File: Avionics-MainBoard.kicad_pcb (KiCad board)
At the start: 4 copper layers, 90.2 x 95.9 mm, 268 parts, among them J1 USB_C_Receptacle_USB2.0, J10 1824543, J11 1824527, J12 1824527, J13 1824527, J14 200528-0100, J15 200528-0100, J16 200528-0100, J17 1824543, J18 200528-0100, J19 200528-0100, J2 200528-0100, J3 Conn_01x06, J4 200528-0100, J5 Micro_SD_Card_Det2, J6 200528-0100, J7 U.FL-R-SMT-1, J8 Conn_01x02, J9 200528-0100, Q1 IRLML2803, Q10 MBT2222ADW1T1, Q11 MBT2222ADW1T1, Q12 MBT2222ADW1T1, Q13 MBT2222ADW1T1, Q14 MMBT2907, Q15 MMBT2907, Q16 NX3008NBKS, Q17 MBT2222ADW1T1, Q2 MBT2222ADW1T1, Q22 NX3008NBKS, Q24 NX3008NBKS, Q26 NX3008NBKS, Q28 NX3008NBKS, Q29 MBT2222ADW1T1, Q3 MBT2222ADW1T1, Q30 MBT2222ADW1T1, Q4 NX3008NBKS, Q44 NX3008NBKS, Q46 NX3008NBKS, Q48 NX3008NBKS, Q5 MBT2222ADW1T1, Q50 NX3008NBKS, Q52 NX3008NBKS, Q6 MBT2222ADW1T1, Q7 MBT2222ADW1T1, Q8 MBT2222ADW1T1, Q9 MBT2222ADW1T1, Q99 NX3008NBKS, SW1 SW_Omron_B3FS, SW2 SW_Omron_B3FS, U1 MR25H40MDF, U10 BTS5090-1EJA, U12 ADM1491EBR, U14 ADM1176-1ARMZ-R7, U15 TPS7A4501DCQT, U16 ADM1176-1ARMZ-R7, U17 TPS54226PWPR, U18 ADM1176-1ARMZ-R7, U2 RP2040, U3 MAX706RESA+, U4 DS3231M, U5 BNO085, U6 USBLC6-2SC6, U7 E22-900M30S, U8 S1216V8, U9 BQ25883RGER, Y1 12MHz, Y2 32.768kHz

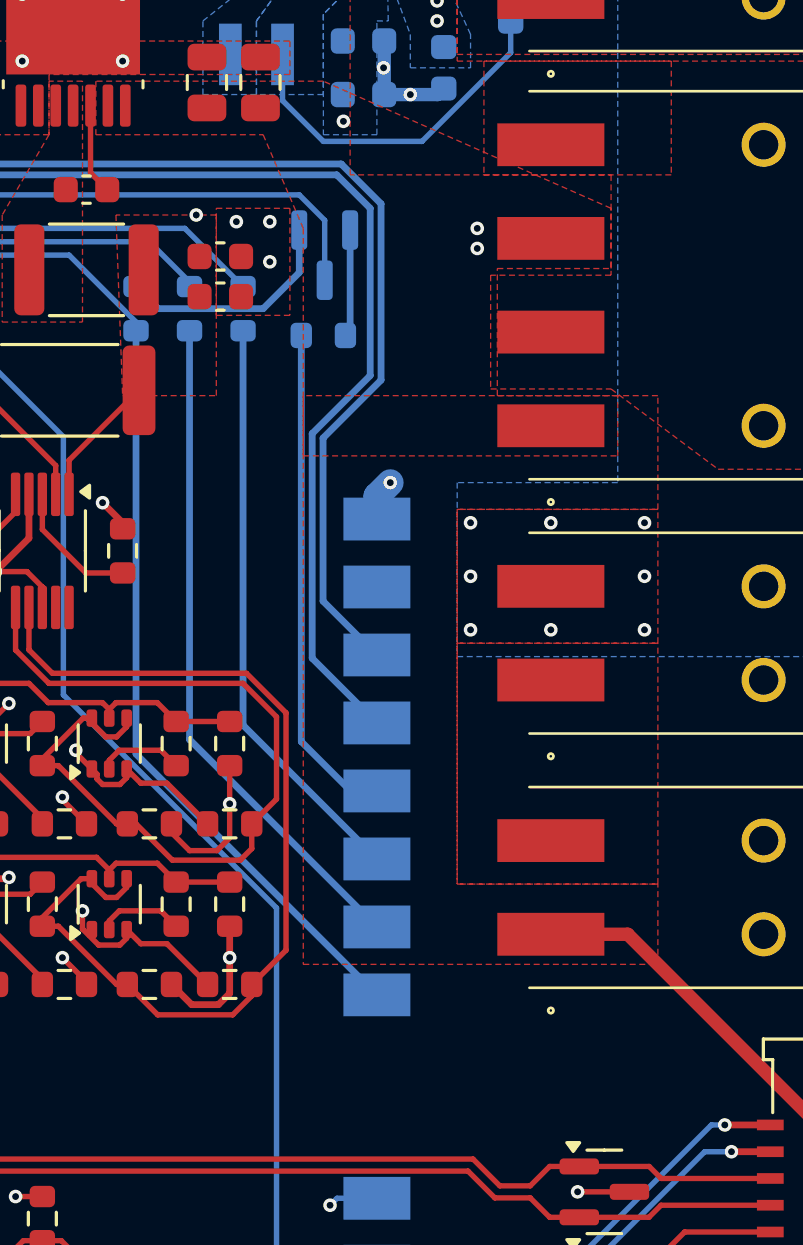
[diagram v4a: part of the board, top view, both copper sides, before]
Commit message: Silkscreen hiding
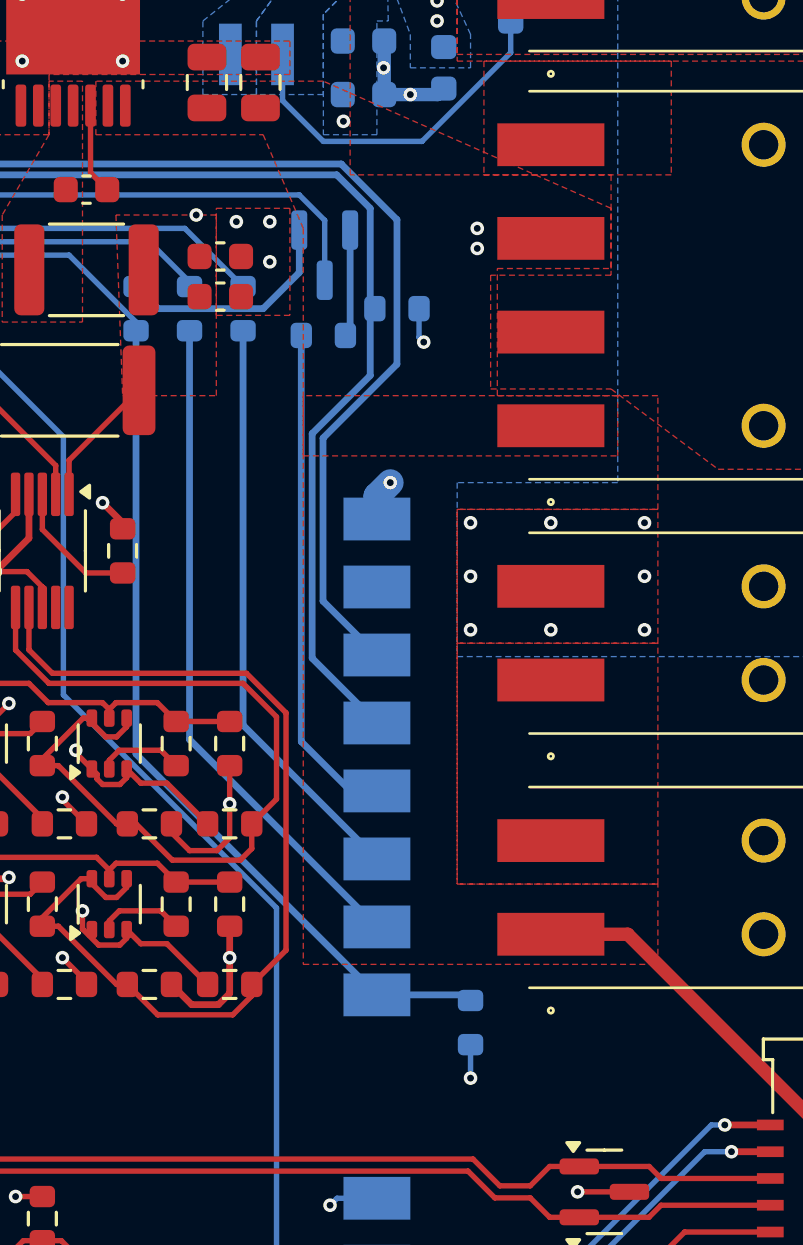
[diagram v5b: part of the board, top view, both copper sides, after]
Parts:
- added R34: 10K, Resistor_SMD:R_0603_1608Metric, B.Cu at (175.2, 95.0)
- added R35: 10K, Resistor_SMD:R_0603_1608Metric, B.Cu at (178.0, 121.7)
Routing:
- net /LoRa Power/LoRa_CSn: track 48.6 -> 52.2 mm
- net +3V3: track 180.1 -> 182.6 mm, vias 65 -> 67

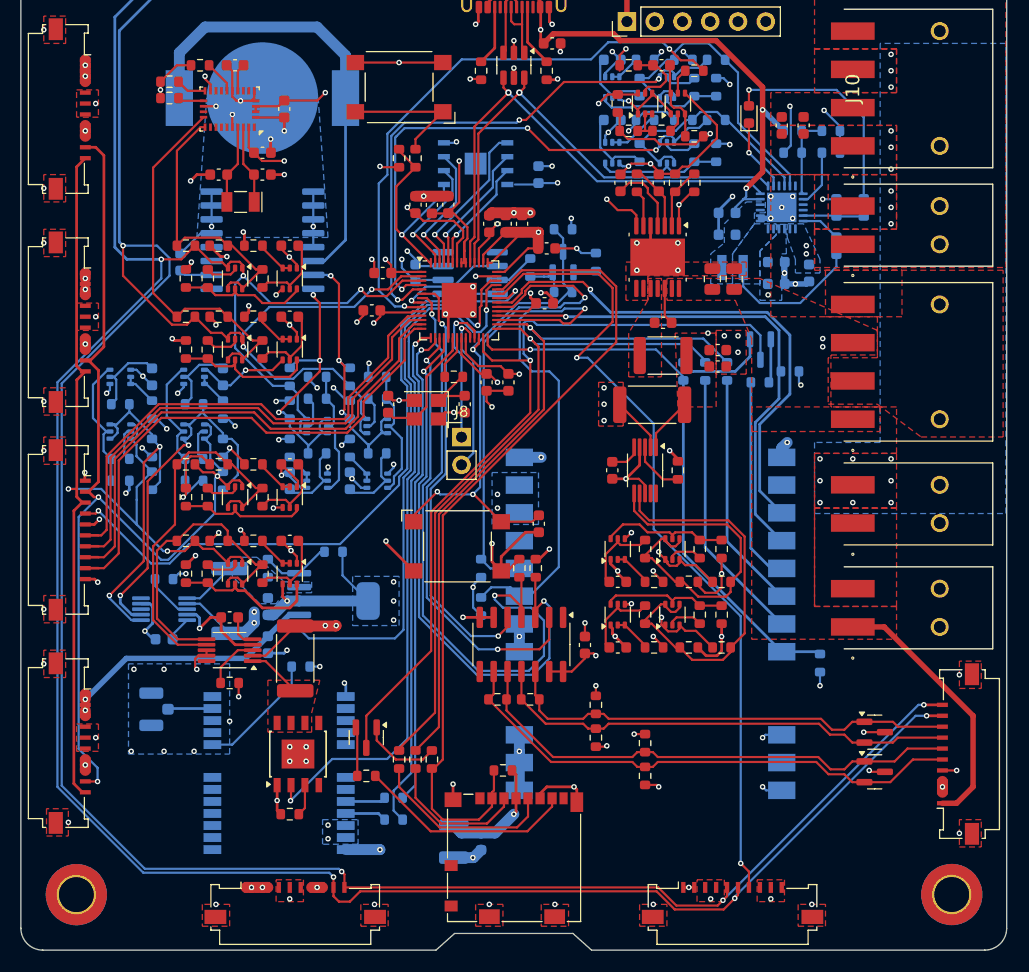
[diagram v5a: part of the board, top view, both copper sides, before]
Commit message: Updated connector locations
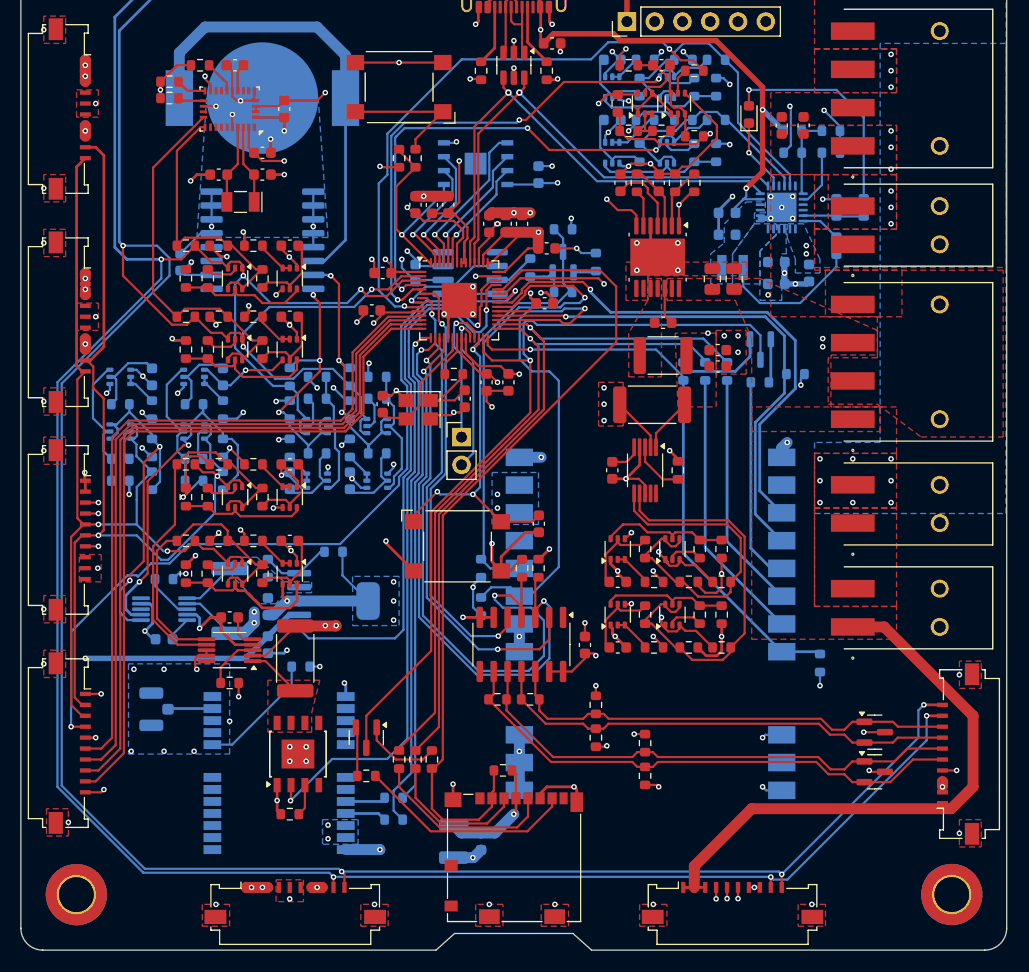
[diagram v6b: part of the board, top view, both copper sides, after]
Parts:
- moved Y1 0.75 mm to (141.2, 98.5)
- moved R34 0.56 mm to (175.8, 95.2)
- moved C1 0.50 mm to (138.0, 98.0)
- moved C2 0.50 mm to (145.5, 97.5)
- moved R2 0.25 mm to (144.5, 95.2)
- moved R25 0.25 mm to (150.8, 113.0)
- moved R26 0.25 mm to (152.2, 113.0)
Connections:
- J15 pad 2: /MCU_IO/I2C1_SDA -> +3V3
- J15 pad 3: /MCU_IO/I2C1_SCL -> GND
- J15 pad 4: /MCU_IO/Jetson_EN -> GND
- J15 pad 5: GND -> /MCU_IO/I2C1_SCL
- J15 pad 6: /MCU_IO/SPI1_MISO -> /MCU_IO/I2C1_SDA
- J15 pad 7: /MCU_IO/Jetson_CSn -> /MCU_IO/Battery_ALERT
- J15 pad 8: /MCU_IO/SPI1_CLK -> GND
- J15 pad 9: /MCU_IO/SPI1_MOSI -> GND
- J16 pad 1: VSYS -> +3V3
- J16 pad 10: /MCU_IO/I2C1_SCL -> GND
- J16 pad 2: VSYS -> /MCU_IO/I2C1_SDA
- J16 pad 3: VSYS -> /MCU_IO/I2C1_SCL
- J16 pad 4: GND -> /MCU_IO/Jetson_EN
- J16 pad 6: GND -> /MCU_IO/SPI1_MISO
- J16 pad 7: +3V3 -> /MCU_IO/Jetson_CSn
- J16 pad 8: +3V3 -> /MCU_IO/SPI1_CLK
- J16 pad 9: /MCU_IO/I2C1_SDA -> /MCU_IO/SPI1_MOSI
- J19 pad 1: +3V3 -> VSYS
- J19 pad 10: GND -> /MCU_IO/I2C0_SDA
- J19 pad 2: +3V3 -> VSYS
- J19 pad 3: GND -> VSYS
- J19 pad 5: /MCU_IO/I2C0_SDA -> GND
- J19 pad 6: /MCU_IO/I2C0_SCL -> GND
- J19 pad 7: /MCU_IO/Battery_ALERT -> +3V3
- J19 pad 8: GND -> +3V3
- J19 pad 9: GND -> /MCU_IO/I2C0_SCL
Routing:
- net VSYS: track 282.7 -> 314.9 mm, vias 16 -> 15
- net /MCU_IO/SPI1_MISO: track 46.3 -> 66.3 mm
- net /MCU_IO/SPI1_MOSI: track 47.9 -> 67.9 mm
- net /MCU_IO/Jetson_CSn: track 47.0 -> 66.8 mm
- net /MCU_IO/SPI1_CLK: track 47.5 -> 67.2 mm
- net /MCU_IO/I2C1_SCL: track 225.6 -> 213.1 mm
- net /MCU_IO/Jetson_EN: track 62.7 -> 74.5 mm
- net /MCU_IO/I2C1_SDA: track 220.5 -> 209.8 mm, vias 7 -> 6
- net GND: track 341.2 -> 348.3 mm, vias 124 -> 127
- net /MCU_IO/Battery_ALERT: track 75.2 -> 80.0 mm
- net +3V3: track 182.6 -> 185.7 mm
- net Net-(C2-Pad2): track 5.69 -> 8.50 mm
- net /MCU_IO/I2C0_SCL: track 282.9 -> 280.8 mm
- net /LoRa Power/I2C Protection3/SCL_DEVICE: track 33.2 -> 32.6 mm
